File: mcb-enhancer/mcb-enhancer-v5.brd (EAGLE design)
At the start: 100 x 44.4 mm, 127 parts, among them T1 BT138-F, T2 BT138-F, T3 BT138-F, T4 BT138-F, T5 BT138-F, T6 BT138-F, T7 BT138-F, T8 BT138-F

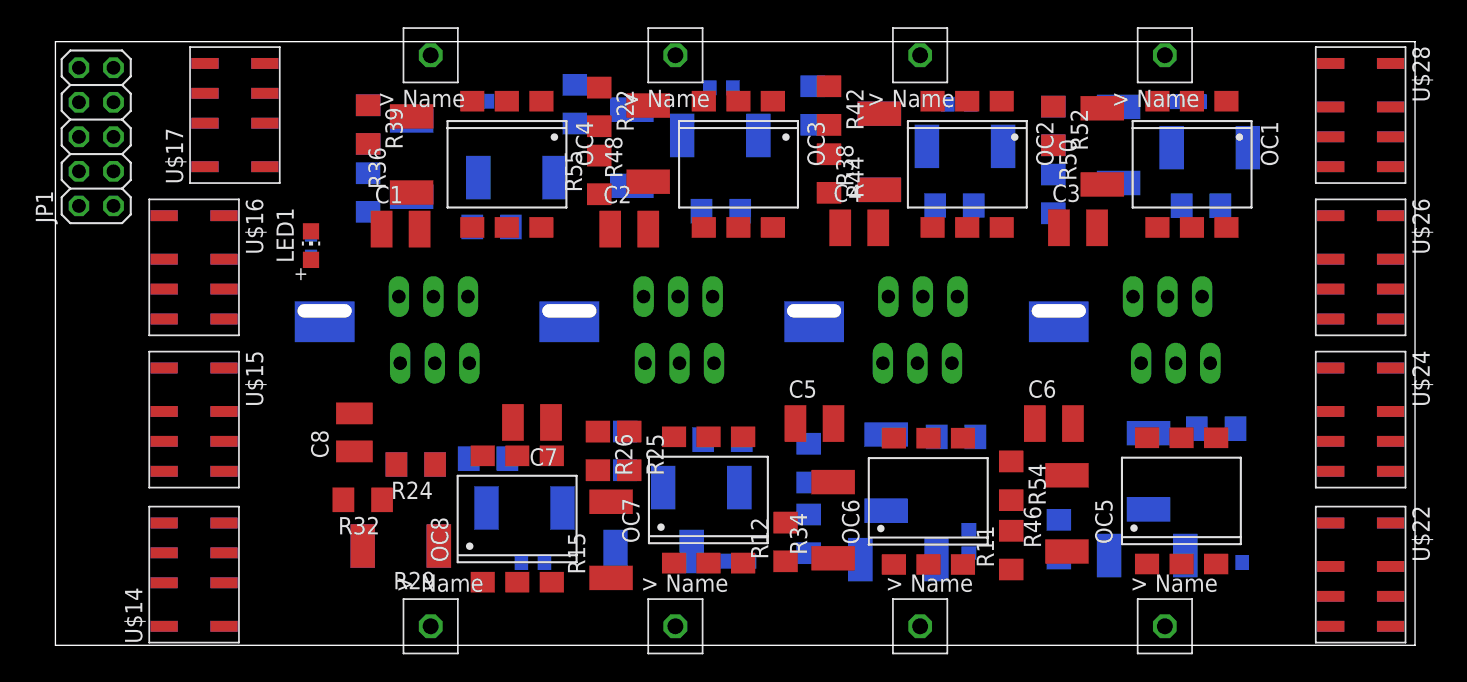
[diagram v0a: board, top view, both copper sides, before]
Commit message: add mcb enhancer BoM and gerber
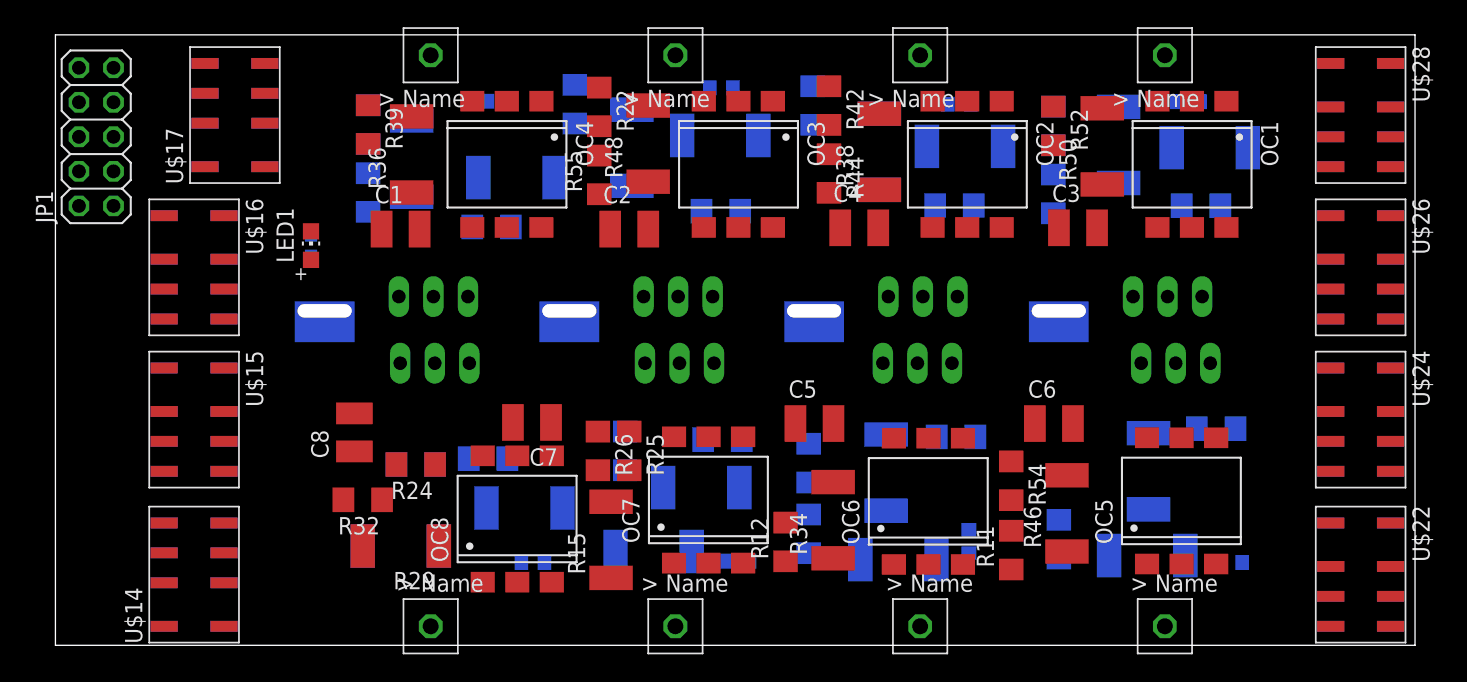
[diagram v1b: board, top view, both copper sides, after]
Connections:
- new net LINE_IN5: U$16.PA, U$16.PB, U$17.PA, U$17.PB, U$20.PA, U$20.PB, U$21.PA, U$21.PB
- new net LINE_IN6: U$22.PA, U$22.PB, U$23.PA, U$23.PB, U$24.PA, U$24.PB, U$25.PA, U$25.PB
- new net LINE_IN6A: U$24.TCA, U$24.TCB, U$25.TCA, U$25.TCB
- new net LINE_IN6B: U$22.TCA, U$22.TCB, U$23.TCA, U$23.TCB
- new net LINE_IN7: U$26.PA, U$26.PB, U$27.PA, U$27.PB, U$28.PA, U$28.PB, U$29.PA, U$29.PB
- new net LINE_IN7A: U$28.TCA, U$28.TCB, U$29.TCA, U$29.TCB
- new net LINE_IN7B: U$26.TCA, U$26.TCB, U$27.TCA, U$27.TCB
- new net LINE_OUT5A: U$17.TCA, U$17.TCB, U$21.TCA, U$21.TCB
- new net LINE_OUT5B: U$16.TCA, U$16.TCB, U$20.TCA, U$20.TCB
- net 5V: now also U$14.V+, U$15.V+, U$16.V+, U$17.V+, U$18.V+, U$19.V+, U$20.V+, U$21.V+, U$22.V+, U$23.V+, U$24.V+, U$25.V+, U$26.V+, U$27.V+, U$28.V+, U$29.V+
- net GND: now also U$14.V-, U$15.V-, U$16.V-, U$17.V-, U$18.V-, U$19.V-, U$20.V-, U$21.V-, U$22.V-, U$23.V-, U$24.V-, U$25.V-, U$26.V-, U$27.V-, U$28.V-, U$29.V-
- net LINE_IN4: now also U$14.PA, U$14.PB, U$15.PA, U$15.PB, U$18.PA, U$18.PB, U$19.PA, U$19.PB
- net LINE_OUT4A: now also U$15.TCA, U$15.TCB, U$19.TCA, U$19.TCB
- net LINE_OUT4B: now also U$14.TCA, U$14.TCB, U$18.TCA, U$18.TCB
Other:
- board size 100 x 44.4 mm -> 100 x 44.9 mm

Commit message: routing mcb-enhancer, not DRC/ERC-ed yet
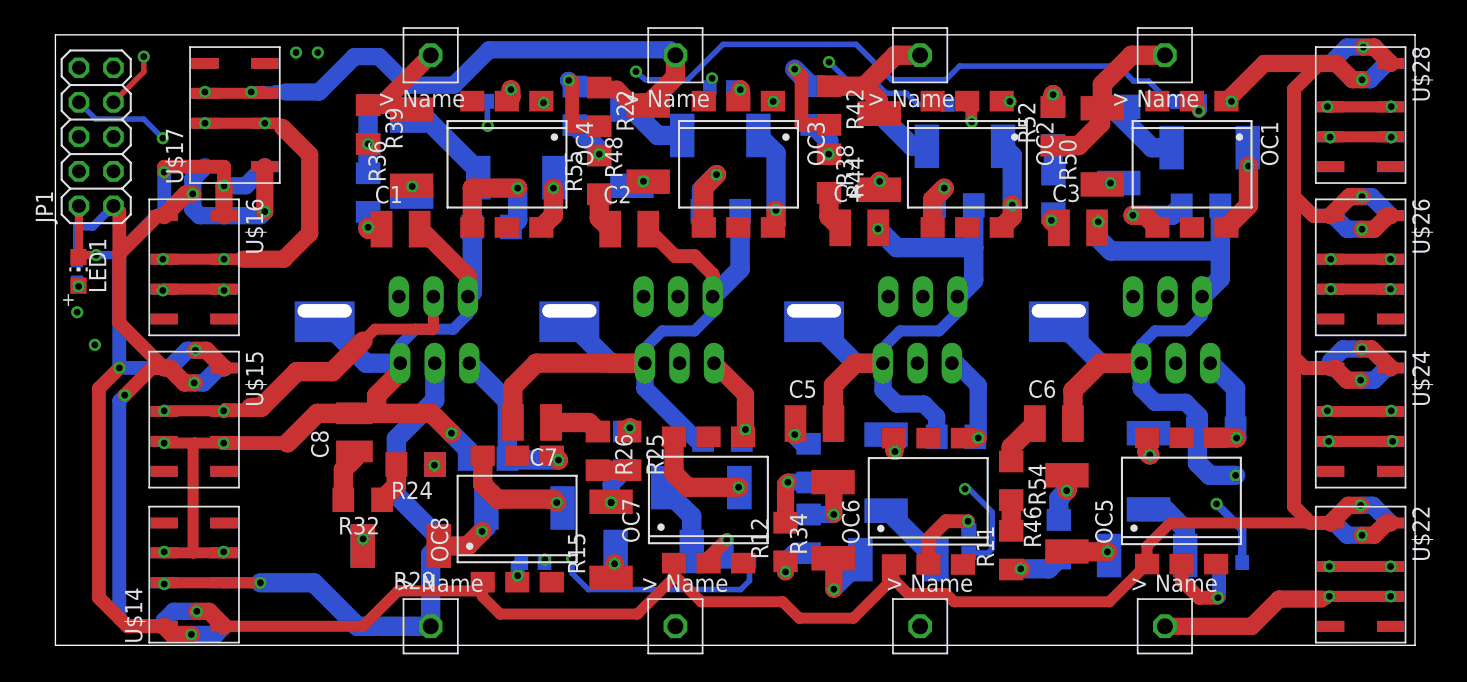
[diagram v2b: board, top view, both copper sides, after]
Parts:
- moved R57 17.3 mm to (1.60, 27.5), turned to 270 degrees
- moved LED1 17.2 mm to (1.70, 27.5)
- moved R36 0.50 mm to (26.2, 36.6)
- moved R51 0.12 mm to (38.2, 39.7)
- moved R52 0.06 mm to (73.3, 38.2), turned to 90 degrees
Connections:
- removed net LINE_IN5: U$16.PA, U$16.PB, U$17.PA, U$17.PB, U$20.PA, U$20.PB, U$21.PA, U$21.PB
- removed net LINE_IN6: U$22.PA, U$22.PB, U$23.PA, U$23.PB, U$24.PA, U$24.PB, U$25.PA, U$25.PB
- removed net LINE_IN6A: U$24.TCA, U$24.TCB, U$25.TCA, U$25.TCB
- removed net LINE_IN6B: U$22.TCA, U$22.TCB, U$23.TCA, U$23.TCB
- removed net LINE_IN7: U$26.PA, U$26.PB, U$27.PA, U$27.PB, U$28.PA, U$28.PB, U$29.PA, U$29.PB
- removed net LINE_IN7A: U$28.TCA, U$28.TCB, U$29.TCA, U$29.TCB
- removed net LINE_IN7B: U$26.TCA, U$26.TCB, U$27.TCA, U$27.TCB
- removed net LINE_OUT5A: U$17.TCA, U$17.TCB, U$21.TCA, U$21.TCB
- removed net LINE_OUT5B: U$16.TCA, U$16.TCB, U$20.TCA, U$20.TCB
- net LINE_IN: now also U$22.TCA, U$22.TCB, U$23.TCA, U$23.TCB, U$24.PA, U$24.PB, U$25.PA, U$25.PB
- net LINE_IN2: now also U$26.TCA, U$26.TCB, U$27.TCA, U$27.TCB, U$28.PA, U$28.PB, U$29.PA, U$29.PB
- net LINE_IN3: now also U$16.TCA, U$16.TCB, U$17.TCA, U$17.TCB, U$20.TCA, U$20.TCB, U$21.TCA, U$21.TCB
- net LINE_OUT2A: now also U$28.TCA, U$28.TCB, U$29.TCA, U$29.TCB
- net LINE_OUT2B: now also U$26.PA, U$26.PB, U$27.PA, U$27.PB
- net LINE_OUT3A: now also U$17.PA, U$17.PB, U$21.PA, U$21.PB
- net LINE_OUT3B: now also U$16.PA, U$16.PB, U$20.PA, U$20.PB
- net LINE_OUTA: now also U$24.TCA, U$24.TCB, U$25.TCA, U$25.TCB
- net LINE_OUTB: now also U$22.PA, U$22.PB, U$23.PA, U$23.PB
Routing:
- net 5V: track 0.00 -> 303.4 mm, vias 0 -> 13
- net GND: track 0.00 -> 233.9 mm, vias 0 -> 10
- net OUT5: track 0.00 -> 120.7 mm, vias 0 -> 2
- net LINE_IN3: track 0.00 -> 116.0 mm, vias 0 -> 4
- net OUT6: track 0.00 -> 108.9 mm, vias 0 -> 1
- net LINE_IN2: track 0.00 -> 93.5 mm, vias 0 -> 5
- net OUT7: track 0.00 -> 90.6 mm, vias 0 -> 2
- net OUT1: track 0.00 -> 89.9 mm, vias 0 -> 2
- net LINE_IN: track 0.00 -> 83.0 mm, vias 0 -> 6
- net OUT8: track 0.00 -> 79.3 mm, vias 0 -> 2
- net OUT2: track 0.00 -> 71.5 mm, vias 0 -> 2
- net LINE_IN4: track 0.00 -> 70.4 mm, vias 0 -> 5
- net LINE_OUT2B: track 0.00 -> 70.3 mm, vias 0 -> 3
- net LINE_OUT3A: track 0.00 -> 67.8 mm, vias 0 -> 2
- net LINE_OUT3B: track 0.00 -> 67.6 mm, vias 0 -> 4
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
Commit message: repair silkscreen
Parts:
- LED1: value (none) -> red
- R57: value (none) -> 270
- R60, R61, R62, R63, R64, R65, R66, R67: value (none) -> 200
- moved C4 0.10 mm to (59.1, 30.6)
- moved C2 0.10 mm to (42.2, 30.5)
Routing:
- net N$47: track 2.85 -> 7.35 mm
- net N$30: track 7.30 -> 8.20 mm
- net LINE_IN3: track 116.0 -> 115.3 mm
